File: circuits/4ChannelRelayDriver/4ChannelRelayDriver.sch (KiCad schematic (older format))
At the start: 11 parts

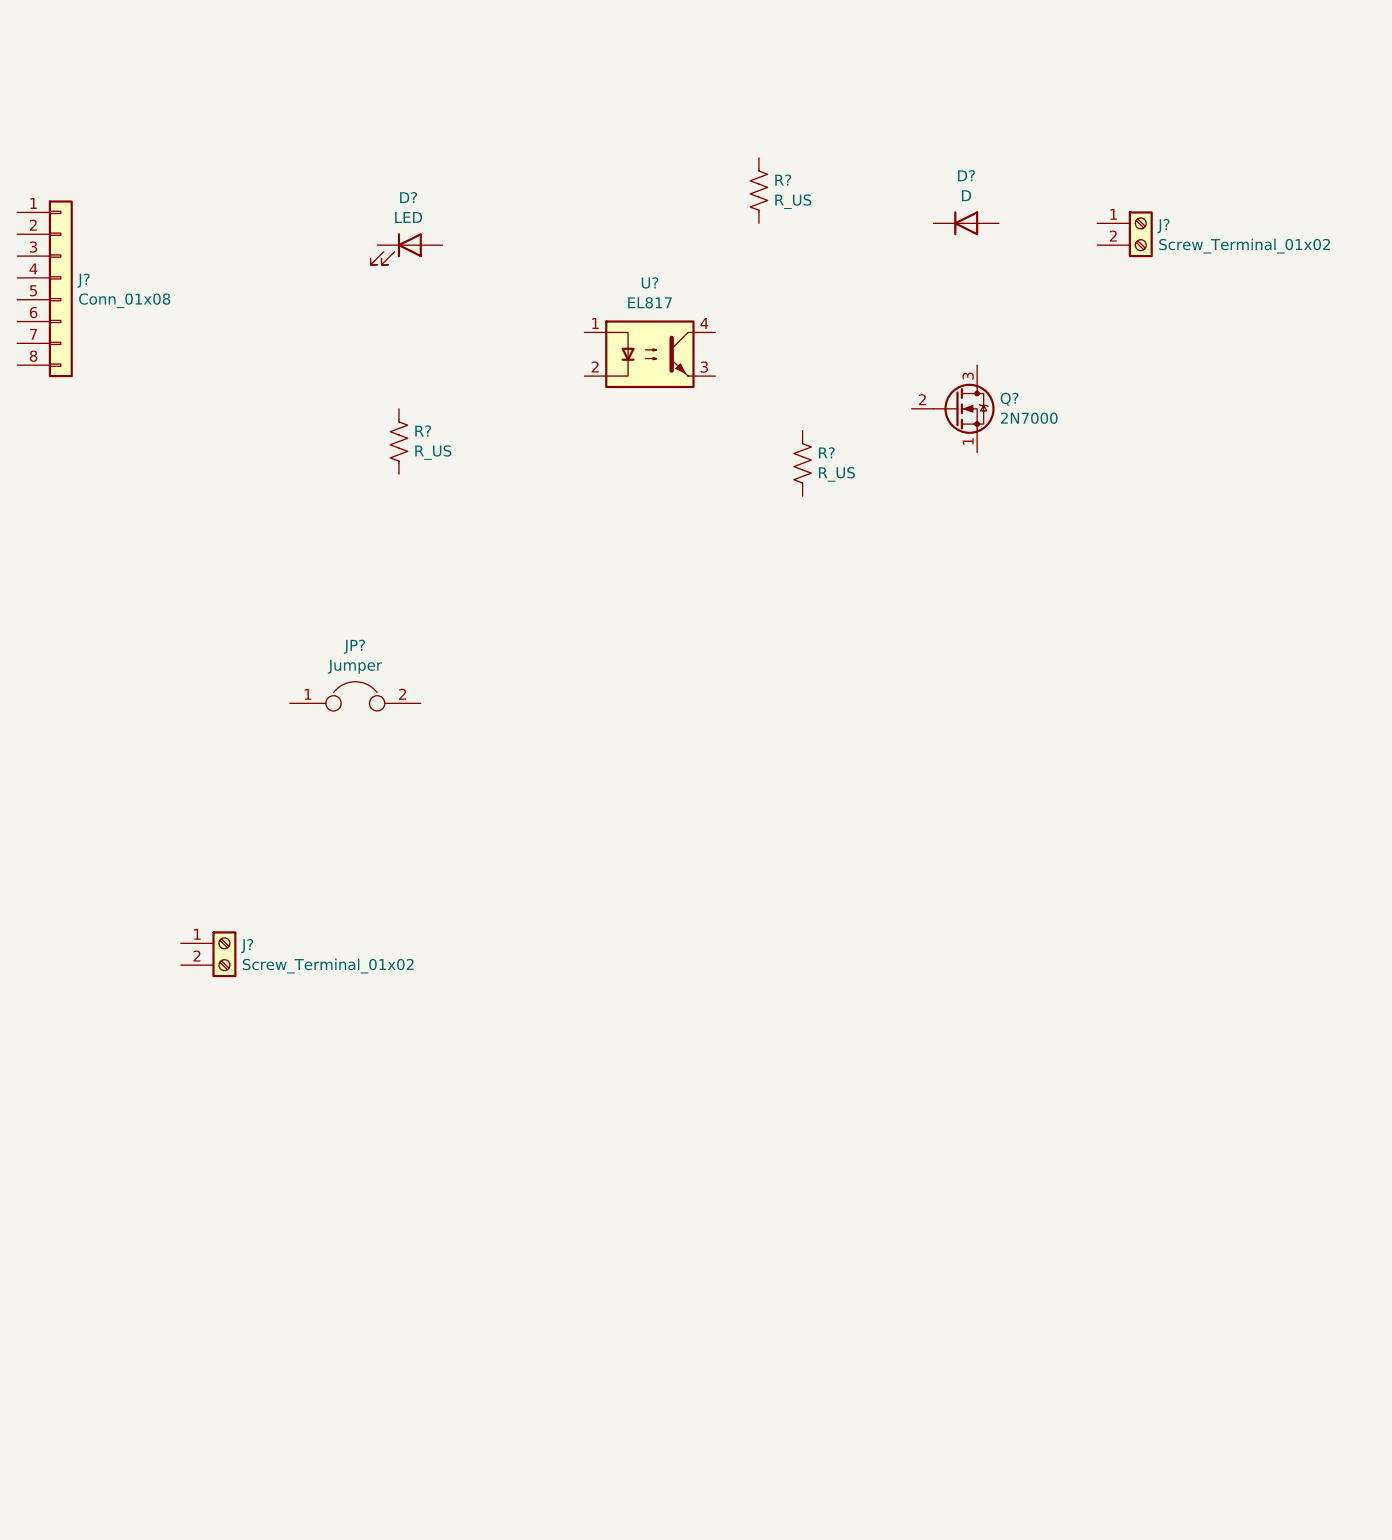
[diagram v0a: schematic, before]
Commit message: Add 4 channel relay driver and start tool builder
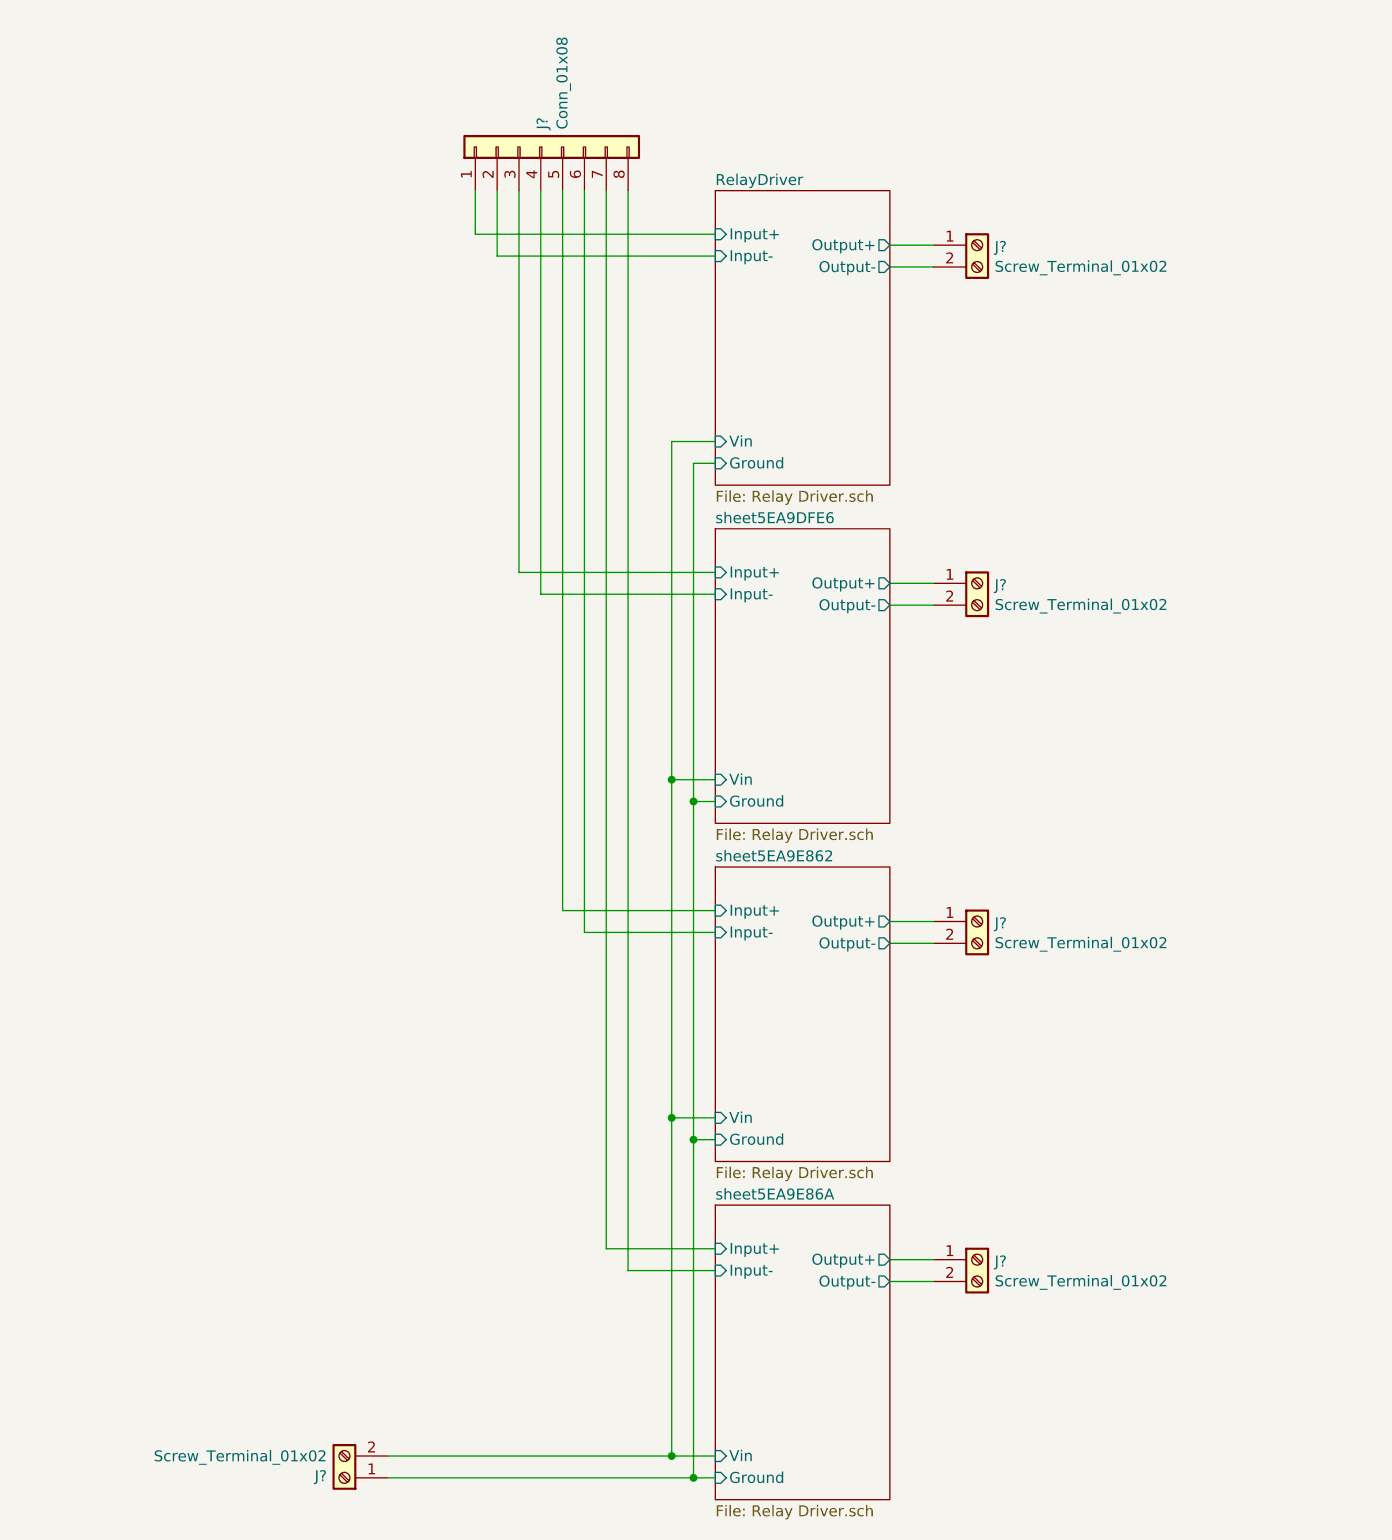
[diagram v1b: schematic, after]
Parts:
- removed D?: LED, symbol Device:LED
- removed D?: D, symbol Device:D
- removed JP?: Jumper, symbol Device:Jumper
- removed Q?: 2N7000, Package_TO_SOT_THT:TO-92_Inline, symbol Transistor_FET:2N7000
- removed R? (x3): R_US, symbol Device:R_US
- removed U?: EL817, Package_DIP:DIP-4_W7.62mm, symbol Isolator:EL817
- added J? (x3): Screw_Terminal_01x02, symbol Connector:Screw_Terminal_01x02
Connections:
- net RelayDriver/Input+: now reaches J?.1 (Pin_1)
- net RelayDriver/Input-: now reaches J?.2 (Pin_2)
- net sheet5EA9DFE6/Input+: now reaches J?.3 (Pin_3)
- net sheet5EA9DFE6/Input-: now reaches J?.4 (Pin_4)
- net sheet5EA9E862/Input+: now reaches J?.5 (Pin_5)
- net sheet5EA9E862/Input-: now reaches J?.6 (Pin_6)
- net sheet5EA9E86A/Input+: now reaches J?.7 (Pin_7)
- net sheet5EA9E86A/Input-: now reaches J?.8 (Pin_8)
- net RelayDriver/Output+: now reaches J?.1 (Pin_1)
- net RelayDriver/Output-: now reaches J?.2 (Pin_2)
- net RelayDriver/Ground: now reaches J?.1 (Pin_1)
- net RelayDriver/Vin: now reaches J?.2 (Pin_2)
- new net sheet5EA9DFE6/Output+: J?.1 (Pin_1)
- new net sheet5EA9DFE6/Output-: J?.2 (Pin_2)
- new net sheet5EA9E862/Output+: J?.1 (Pin_1)
- new net sheet5EA9E862/Output-: J?.2 (Pin_2)
- new net sheet5EA9E86A/Output+: J?.1 (Pin_1)
- new net sheet5EA9E86A/Output-: J?.2 (Pin_2)
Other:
- moved on the sheet: J?
